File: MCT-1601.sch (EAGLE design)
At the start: 14 parts, among them J1 DUT, J2 Button, J3 D I/O, J5 A In, J6 Pwr, Q1 BC327

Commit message: Add files via upload
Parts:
- removed RLY1: W171-DIP-28, 00 Nik misc:W171-DIP-28
- added D1: (no value), diode:DIODE-D-2.5
- added K1: 351, relay:351
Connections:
- new net N$1: J1.2, K13.P
- new net N$4: J1.1, K12.P
- net N$3: now also D1.A, K11.2; no longer RLY1.-
- net T1: now also K12.S; no longer J1.1, RLY1.NC2A@1, RLY1.NC2A@2
- net T2: now also K13.S; no longer J1.2, RLY1.NC1A
- net T3: now also K12.O, K13.O; no longer RLY1.NC1B, RLY1.NC2B@1, RLY1.NC2B@2
- net VCC: now also D1.C, K11.1; no longer RLY1.+
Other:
- moved on the sheet: J1, J2, J3, J5, J6, Q1, R1, R2, R3, R4, R5, R6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

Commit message: Add files via upload
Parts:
- added R8, R9: 10R, SparkFun-Resistors:1KOHM-1/4W-1%(PTH)VERT
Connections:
- new net N$5: K12.O, R8.2
- new net N$6: K13.O, R9.2
- net T3: now also R8.1, R9.1; no longer K12.O, K13.O
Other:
- moved on the sheet: D1, J1, J2, K1, Q1

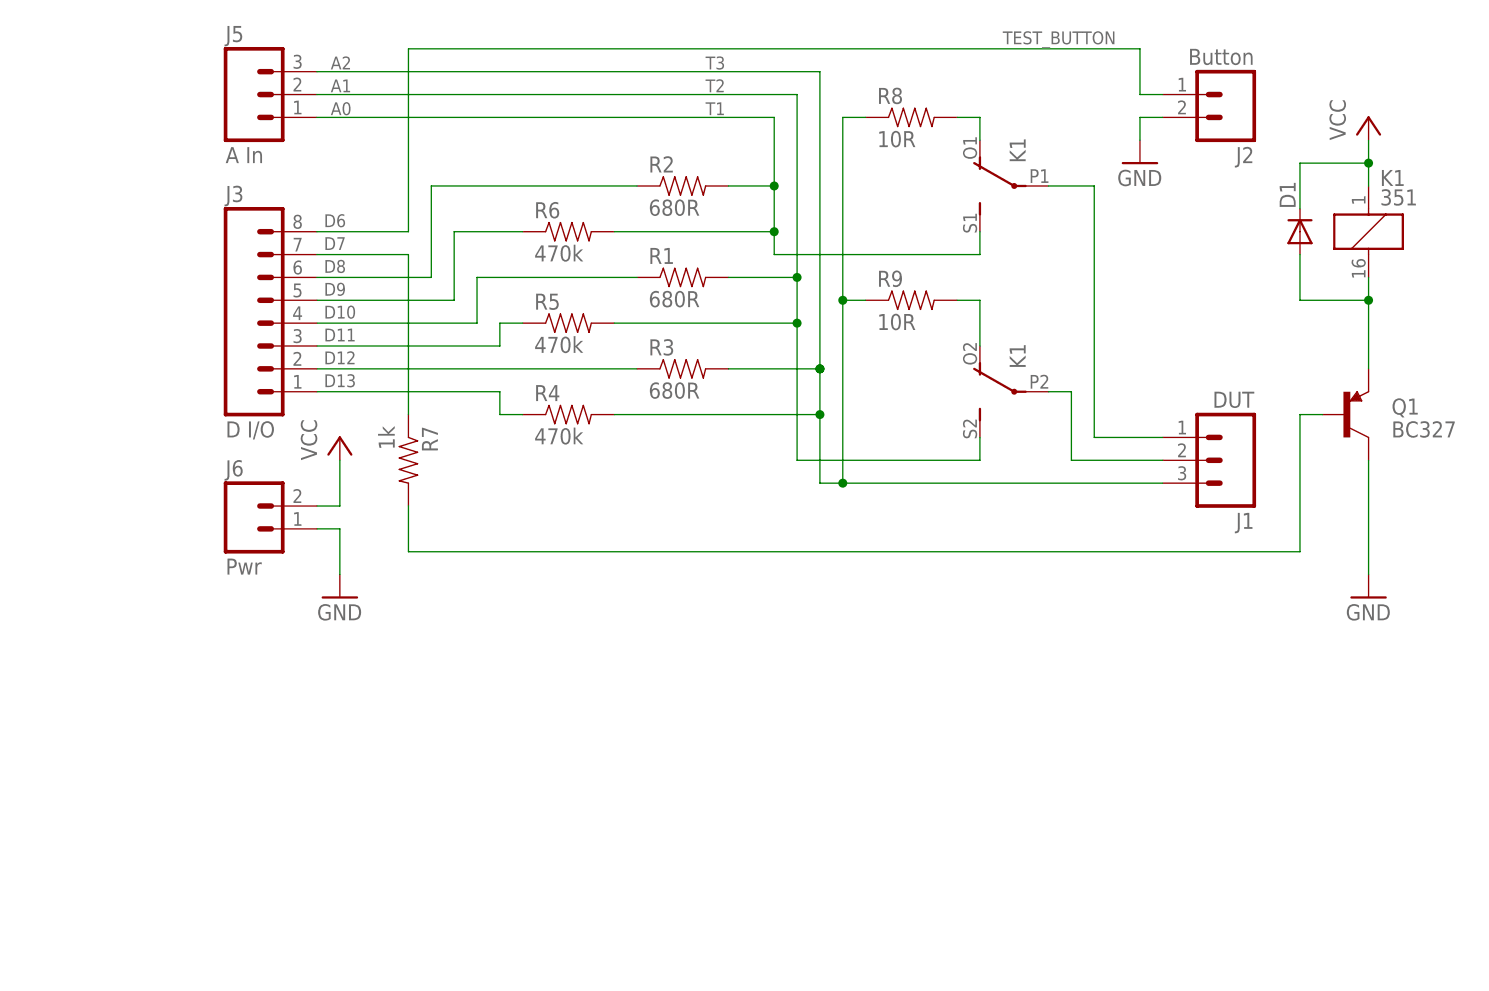
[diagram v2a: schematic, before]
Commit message: Modified to support autodiagnostics on startup
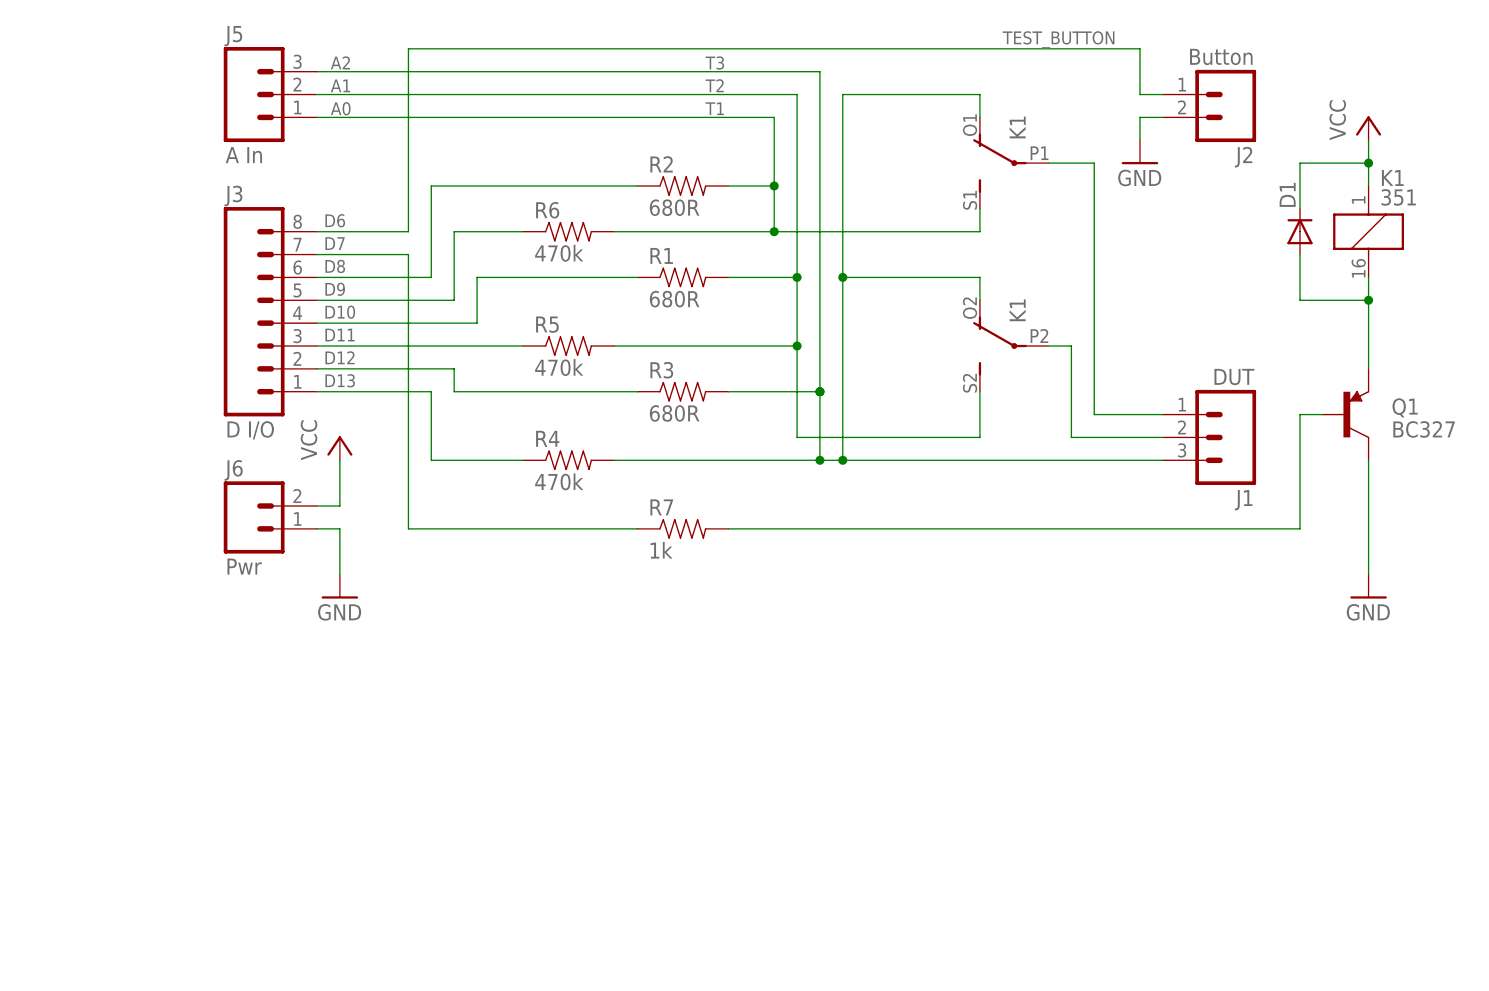
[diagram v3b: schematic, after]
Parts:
- removed R8, R9: 10R, SparkFun-Resistors:1KOHM-1/4W-1%(PTH)VERT
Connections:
- removed net N$5: K12.O, R8.2
- removed net N$6: K13.O, R9.2
- net T3: now also K12.O, K13.O; no longer R8.1, R9.1
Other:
- moved on the sheet: J1, K1, R3, R4, R5, R7

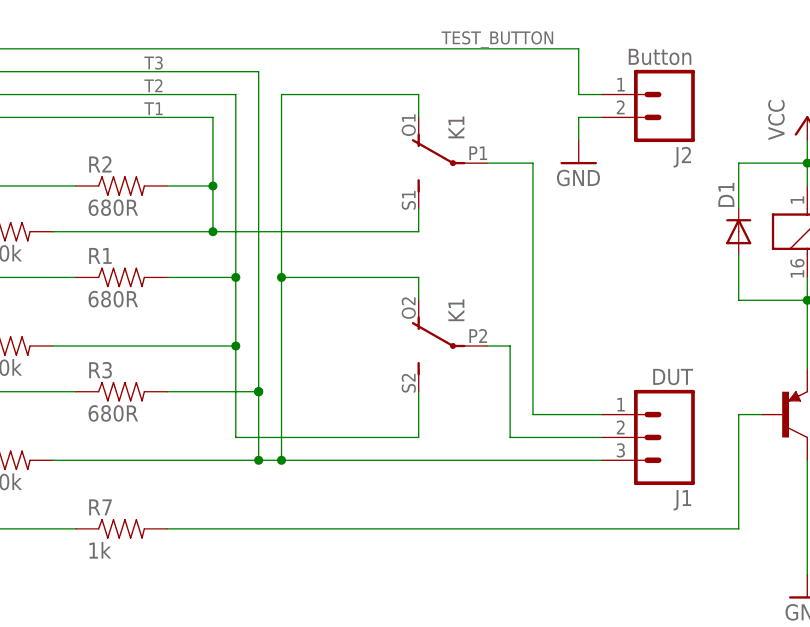
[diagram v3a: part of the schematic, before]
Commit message: Adding correct ec2 verion
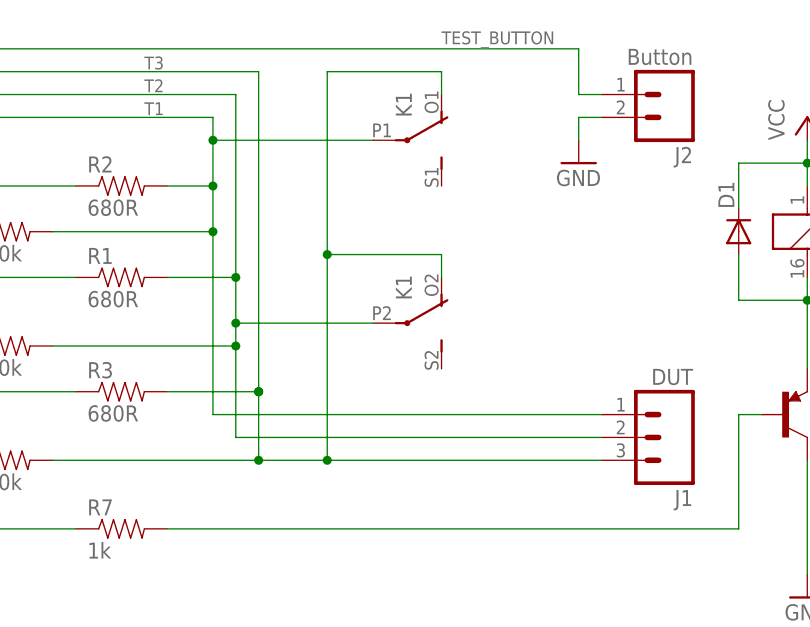
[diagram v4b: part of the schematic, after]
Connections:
- removed net N$1: J1.2, K13.P
- removed net N$4: J1.1, K12.P
- net T1: now also J1.1, K12.P; no longer K12.S
- net T2: now also J1.2, K13.P; no longer K13.S
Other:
- moved on the sheet: K1
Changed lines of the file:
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@@
 <instance part="J3" gate="G$1" x="68.58" y="60.96"/>
 <instance part="K1" gate="1" x="190.5" y="71.12"/>
-<instance part="K1" gate="2" x="152.4" y="78.74" rot="R90"/>
-<instance part="K1" gate="3" x="152.4" y="58.42" rot="R90"/>
+<instance part="K1" gate="2" x="144.78" y="81.28" rot="MR90"/>
+<instance part="K1" gate="3" x="144.78" y="60.96" rot="MR90"/>
 <instance part="D1" gate="G$1" x="182.88" y="71.12" rot="R90"/>
 </instances>
@@
 <pinref part="R6" gate="G$1" pin="2"/>
 <wire x1="106.68" y1="71.12" x2="124.46" y2="71.12" width="0.1524" layer="91"/>
-<wire x1="124.46" y1="76.2" x2="124.46" y2="83.82" width="0.1524" layer="91"/>
+<wire x1="124.46" y1="76.2" x2="124.46" y2="81.28" width="0.1524" layer="91"/>
 <junction x="124.46" y="76.2"/>
+<wire x1="124.46" y1="81.28" x2="124.46" y2="83.82" width="0.1524" layer="91"/>
 <wire x1="73.66" y1="83.82" x2="124.46" y2="83.82" width="0.1524" layer="91"/>
 <pinref part="J5" gate="J$1" pin="1"/>
 <label x="116.84" y="84.074" size="1.4224" layer="95"/>
-<pinref part="K1" gate="2" pin="S"/>
-<wire x1="147.32" y1="73.66" x2="147.32" y2="71.12" width="0.1524" layer="91"/>
-<wire x1="124.46" y1="71.12" x2="147.32" y2="71.12" width="0.1524" layer="91"/>
+<pinref part="K1" gate="2" pin="P"/>
+<wire x1="142.24" y1="81.28" x2="124.46" y2="81.28" width="0.1524" layer="91"/>
+<junction x="124.46" y="81.28"/>
+<pinref part="J1" gate="J$1" pin="1"/>
+<wire x1="167.64" y1="50.8" x2="124.46" y2="50.8" width="0.1524" layer="91"/>
+<wire x1="124.46" y1="50.8" x2="124.46" y2="71.12" width="0.1524" layer="91"/>
 <junction x="124.46" y="71.12"/>
 </segment>
@@
 <net name="T2" class="0">
 <segment>
-<wire x1="127" y1="48.26" x2="127" y2="58.42" width="0.1524" layer="91"/>
 <pinref part="R1" gate="G$1" pin="2"/>
-<wire x1="127" y1="58.42" x2="127" y2="66.04" width="0.1524" layer="91"/>
+<wire x1="127" y1="58.42" x2="127" y2="60.96" width="0.1524" layer="91"/>
+<wire x1="127" y1="60.96" x2="127" y2="66.04" width="0.1524" layer="91"/>
 <wire x1="127" y1="66.04" x2="119.38" y2="66.04" width="0.1524" layer="91"/>
 <wire x1="127" y1="66.04" x2="127" y2="86.36" width="0.1524" layer="91"/>
@@
 <pinref part="J5" gate="J$1" pin="2"/>
 <label x="116.84" y="86.614" size="1.4224" layer="95"/>
-<pinref part="K1" gate="3" pin="S"/>
-<wire x1="147.32" y1="53.34" x2="147.32" y2="48.26" width="0.1524" layer="91"/>
-<wire x1="147.32" y1="48.26" x2="127" y2="48.26" width="0.1524" layer="91"/>
 <pinref part="R5" gate="G$1" pin="2"/>
 <wire x1="106.68" y1="58.42" x2="127" y2="58.42" width="0.1524" layer="91"/>
+<pinref part="K1" gate="3" pin="P"/>
+<wire x1="142.24" y1="60.96" x2="127" y2="60.96" width="0.1524" layer="91"/>
+<junction x="127" y="60.96"/>
+<pinref part="J1" gate="J$1" pin="2"/>
+<wire x1="167.64" y1="48.26" x2="127" y2="48.26" width="0.1524" layer="91"/>
+<wire x1="127" y1="48.26" x2="127" y2="58.42" width="0.1524" layer="91"/>
 <junction x="127" y="58.42"/>
 </segment>
@@
 <wire x1="119.38" y1="53.34" x2="129.54" y2="53.34" width="0.1524" layer="91"/>
 <junction x="129.54" y="53.34"/>
+<junction x="129.54" y="53.34"/>
 <wire x1="129.54" y1="53.34" x2="129.54" y2="88.9" width="0.1524" layer="91"/>
-<junction x="129.54" y="53.34"/>
 <wire x1="73.66" y1="88.9" x2="129.54" y2="88.9" width="0.1524" layer="91"/>
 <pinref part="J5" gate="J$1" pin="3"/>
 <label x="116.84" y="89.154" size="1.4224" layer="95"/>
 <pinref part="J1" gate="J$1" pin="3"/>
-<wire x1="167.64" y1="45.72" x2="132.08" y2="45.72" width="0.1524" layer="91"/>
-<wire x1="132.08" y1="86.36" x2="132.08" y2="66.04" width="0.1524" layer="91"/>
-<junction x="132.08" y="45.72"/>
-<wire x1="132.08" y1="66.04" x2="132.08" y2="45.72" width="0.1524" layer="91"/>
-<wire x1="132.08" y1="45.72" x2="129.54" y2="45.72" width="0.1524" layer="91"/>
+<wire x1="167.64" y1="45.72" x2="137.16" y2="45.72" width="0.1524" layer="91"/>
+<junction x="137.16" y="45.72"/>
+<wire x1="137.16" y1="88.9" x2="137.16" y2="68.58" width="0.1524" layer="91"/>
+<wire x1="137.16" y1="68.58" x2="137.16" y2="45.72" width="0.1524" layer="91"/>
+<wire x1="137.16" y1="45.72" x2="129.54" y2="45.72" width="0.1524" layer="91"/>
 <junction x="129.54" y="45.72"/>
-<junction x="132.08" y="66.04"/>
+<pinref part="K1" gate="3" pin="O"/>
+<wire x1="149.86" y1="66.04" x2="149.86" y2="68.58" width="0.1524" layer="91"/>
+<wire x1="149.86" y1="68.58" x2="137.16" y2="68.58" width="0.1524" layer="91"/>
+<junction x="137.16" y="68.58"/>
 <pinref part="K1" gate="2" pin="O"/>
-<wire x1="147.32" y1="83.82" x2="147.32" y2="86.36" width="0.1524" layer="91"/>
-<wire x1="132.08" y1="86.36" x2="147.32" y2="86.36" width="0.1524" layer="91"/>
-<pinref part="K1" gate="3" pin="O"/>
-<wire x1="147.32" y1="66.04" x2="147.32" y2="63.5" width="0.1524" layer="91"/>
-<wire x1="132.08" y1="66.04" x2="147.32" y2="66.04" width="0.1524" layer="91"/>
+<wire x1="137.16" y1="88.9" x2="149.86" y2="88.9" width="0.1524" layer="91"/>
+<wire x1="149.86" y1="88.9" x2="149.86" y2="86.36" width="0.1524" layer="91"/>
 </segment>
 </net>
@@
 </segment>
 </net>
-<net name="N$1" class="0">
-<segment>
-<pinref part="J1" gate="J$1" pin="2"/>
-<wire x1="167.64" y1="48.26" x2="157.48" y2="48.26" width="0.1524" layer="91"/>
-<wire x1="157.48" y1="48.26" x2="157.48" y2="58.42" width="0.1524" layer="91"/>
-<pinref part="K1" gate="3" pin="P"/>
-<wire x1="157.48" y1="58.42" x2="154.94" y2="58.42" width="0.1524" layer="91"/>
-</segment>
-</net>
-<net name="N$4" class="0">
-<segment>
-<pinref part="K1" gate="2" pin="P"/>
-<wire x1="154.94" y1="78.74" x2="160.02" y2="78.74" width="0.1524" layer="91"/>
-<wire x1="160.02" y1="78.74" x2="160.02" y2="50.8" width="0.1524" layer="91"/>
-<pinref part="J1" gate="J$1" pin="1"/>
-<wire x1="160.02" y1="50.8" x2="167.64" y2="50.8" width="0.1524" layer="91"/>
-</segment>
-</net>

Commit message: Added diode value
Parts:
- D1: value (none) -> 1N4148
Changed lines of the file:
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@@
 <part name="J3" library="SparkFun-Connectors" deviceset="M08" device="" value="D I/O"/>
 <part name="K1" library="relay" deviceset="351" device=""/>
-<part name="D1" library="diode" deviceset="DIODE-" device="D-2.5"/>
+<part name="D1" library="diode" deviceset="DIODE-" device="D-2.5" value="1N4148"/>
 </parts>
 <sheets>
@@
 <instance part="K1" gate="2" x="144.78" y="81.28" rot="MR90"/>
 <instance part="K1" gate="3" x="144.78" y="60.96" rot="MR90"/>
-<instance part="D1" gate="G$1" x="182.88" y="71.12" rot="R90"/>
+<instance part="D1" gate="G$1" x="182.88" y="71.12" smashed="yes" rot="R90">
+<attribute name="NAME" x="183.642" y="73.8886" size="1.778" layer="95"/>
+<attribute name="VALUE" x="181.1274" y="66.802" size="1.778" layer="96" rot="R90"/>
+</instance>
 </instances>
 <busses>
